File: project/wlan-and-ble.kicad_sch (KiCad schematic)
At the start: 0 parts

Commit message: Added CubeMX project and some schematic components are added
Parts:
- added C12: 10u, symbol Device:C
- added C13: 22u, symbol Device:C
- added C14: 0.1u, symbol Device:C
- added C15: TBD, symbol Device:C
- added D1: TBD, symbol Device:D
- added IC1: ESP32-C61-WROOM-1-N8R2, ESP32C61WROOM1N8R2, symbol bozi:ESP32-C61-WROOM-1-N8R2
- added R3: TBD, symbol Device:R
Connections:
- new net DEBUG_RX: IC1.24 (RX0)
- new net DEBUG_TX: IC1.25 (TX0)
- new net EN: C15.1, IC1.3 (EN), R3.2
- new net GND: C12.2, C13.2, C14.2, C15.2, D1.2 (A), IC1.1 (GND_1), IC1.28 (GND_2), IC1.29 (GND_3), IC1.30 (GND_4), IC1.31 (GND_5), IC1.32 (GND_6), IC1.33 (GND_7), IC1.34 (GND_8), IC1.35 (GND_9), IC1.36 (GND_10), IC1.37 (GND_11)
- new net VDD_3V3: C12.1, C13.1, C14.1, D1.1 (K), IC1.2 (3V3), R3.1
- no-connect marks 0 -> 2
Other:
- note added: "SPI and UART are to be defined (TBD)"

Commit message: schemtic is done, need to go through BOM
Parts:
- added R2: 0R, bozi:RESC1005X37N_edit, symbol Device:R
- C15: renamed from C12; value 10u -> 10uF; footprint (none) -> bozi:GRT18_T15; Manufacturer_Name (none) -> Murata Electronics; Manufacturer_Part_Number (none) -> GRT188R61A106KE13D
- C16: renamed from C13; value 22u -> 22uF; footprint (none) -> bozi:GRM18_T20; Manufacturer_Name (none) -> Murata Electronics; Manufacturer_Part_Number (none) -> GRM188R60J226MEA0D
- C17: renamed from C14; value 0.1u -> 100nF; footprint (none) -> bozi:GRM18_T10; Manufacturer_Name (none) -> Murata Electronics; Manufacturer_Part_Number (none) -> GRM188R71H104KA93D
- C18: renamed from C15; Manufacturer_Name (none) -> Murata Electronics
- IC1: footprint ESP32C61WROOM1N8R2 -> bozi:ESP32C61WROOM1N8R2_edit
- R7: renamed from R3; Manufacturer_Name (none) -> Yageo
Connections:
- net SPI2_CLK: now also IC1.18 (IO27)
- net SPI2_CSN: now also IC1.16 (IO25)
- net SPI2_MISO: now also IC1.15 (IO9)
- net SPI2_MOSI: now also IC1.17 (IO26)
- net VDD_3V3: now also R2.1; no longer C16.1, C17.1, IC1.2 (3V3)
- new net: C16.1, C17.1, IC1.2 (3V3), R2.2
- no-connect marks 2 -> 18
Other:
- moved on the sheet: C15, D1

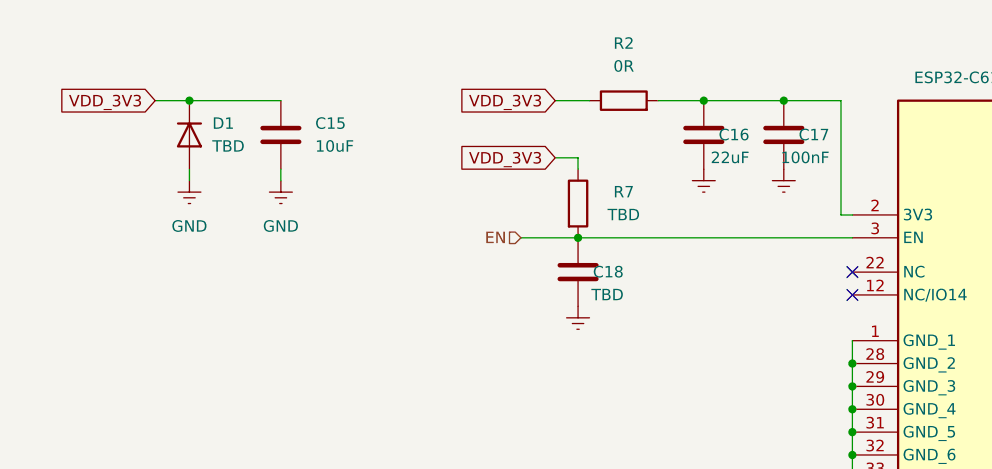
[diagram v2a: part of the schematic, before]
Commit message: schemtic is done, annotation set
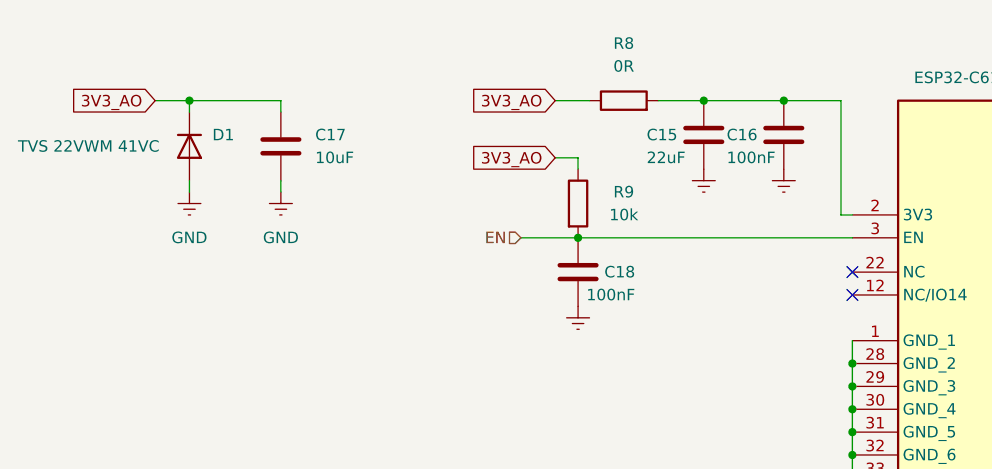
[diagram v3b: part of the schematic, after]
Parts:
- C18: value TBD -> 100nF; footprint (none) -> bozi:GRM18_T10; Manufacturer_Part_Number (none) -> GRM188R71H104KA93D
- D1: value TBD -> TVS 22VWM 41VC; footprint (none) -> bozi:ESDA25P351U1M_edit; Manufacturer_Name (none) -> STMicroelectronics; Manufacturer_Part_Number (none) -> ESDA25P35-1U1M
- R9: renamed from R7; value TBD -> 10k; footprint (none) -> bozi:RESC1005X37N_edit; Manufacturer_Name Yageo -> YAGEO; Manufacturer_Part_Number (none) -> RT0402FRD0710KL
- renumbered C16 to C15, C17 to C16, C15 to C17, R2 to R8
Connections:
- net VDD_3V3 renamed 3V3_AO
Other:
- moved on the sheet: C17, D1
